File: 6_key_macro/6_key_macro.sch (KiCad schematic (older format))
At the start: 37 parts, among them J1 SWD, P1 USB_C_Plug_USB2.0, Q1 DMG1012T, SW1 CherryMX_LED, SW2 CherryMX_LED, SW3 CherryMX_LED, SW4 CherryMX_LED, SW5 CherryMX_LED, SW6 CherryMX_LED, SW7 Boot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

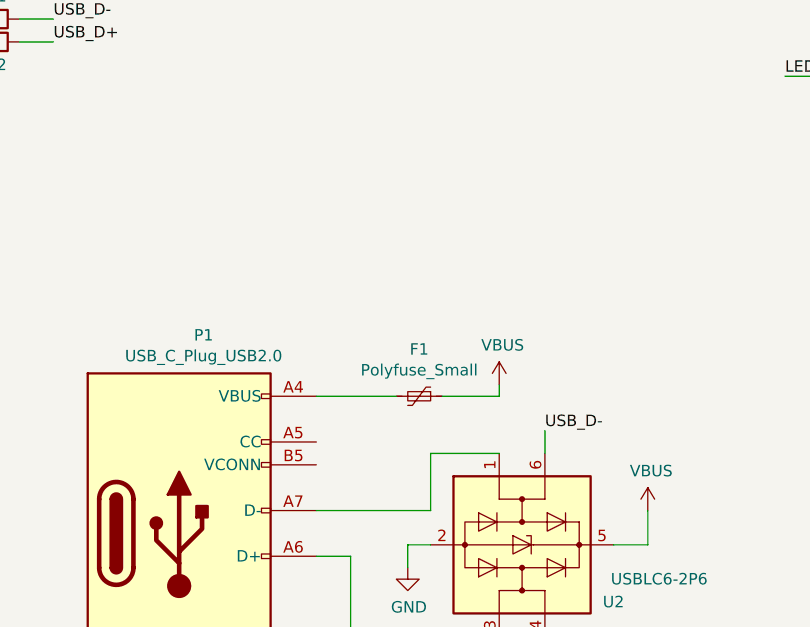
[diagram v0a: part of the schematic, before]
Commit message: added 5.1k resistors to cc1 and cc2 for usb-c to usb-c compatibility
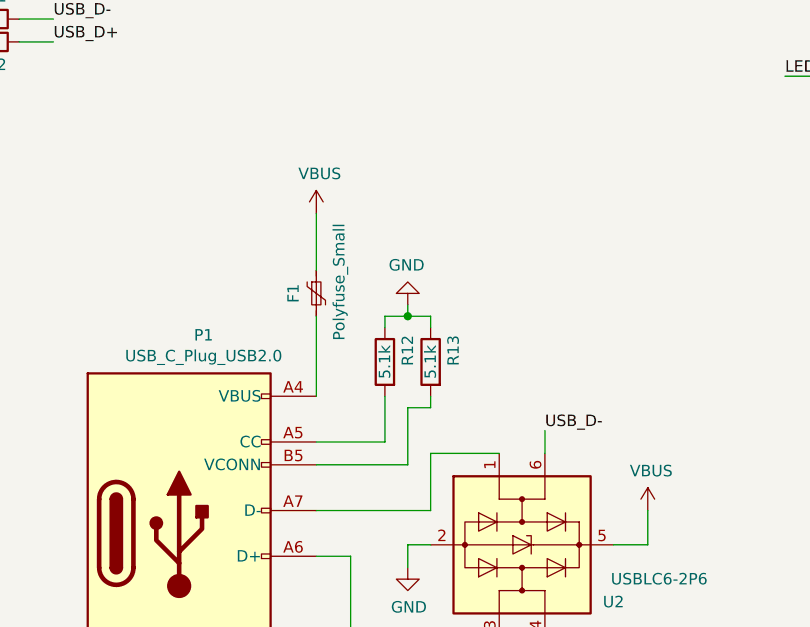
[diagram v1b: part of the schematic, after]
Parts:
- added R12, R13: 5.1k, Resistor_SMD:R_0805_2012Metric_Pad1.20x1.40mm_HandSolder, symbol Device:R
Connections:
- net GND: now also R12.1, R13.1
- net at P1.A5 (CC): now also R12.2
- net at P1.B5 (VCONN): now also R13.2
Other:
- moved on the sheet: F1
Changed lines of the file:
@@
 USB_D+
 Wire Wire Line
-	4400 5700 4750 5700
+	4400 5700 4400 5350
 $Comp
 L power:VBUS #PWR0109
 U 1 1 614AC2B7
-P 5200 5650
-F 0 "#PWR0109" H 5200 5500 50  0001 C CNN
-F 1 "VBUS" H 5215 5823 50  0000 C CNN
-F 2 "" H 5200 5650 50  0001 C CNN
-F 3 "" H 5200 5650 50  0001 C CNN
-	1    5200 5650
+P 4400 4900
+F 0 "#PWR0109" H 4400 4750 50  0001 C CNN
+F 1 "VBUS" H 4415 5073 50  0000 C CNN
+F 2 "" H 4400 4900 50  0001 C CNN
+F 3 "" H 4400 4900 50  0001 C CNN
+	1    4400 4900
 	1    0    0    -1
 $EndComp
@@
 L Device:Polyfuse_Small F1
 U 1 1 614F2940
-P 4850 5700
-F 0 "F1" V 4645 5700 50  0000 C CNN
-F 1 "Polyfuse_Small" V 4736 5700 50  0000 C CNN
-F 2 "Fuse:Fuse_0805_2012Metric_Pad1.15x1.40mm_HandSolder" H 4900 5500 50  0001 L CNN
-F 3 "~" H 4850 5700 50  0001 C CNN
-	1    4850 5700
-	0    1    1    0
-$EndComp
-Wire Wire Line
-	5200 5650 5200 5700
-Wire Wire Line
-	5200 5700 4950 5700
+P 4400 5250
+F 0 "F1" V 4300 5250 50  0000 C CNN
+F 1 "Polyfuse_Small" V 4500 5300 50  0000 C CNN
+F 2 "Fuse:Fuse_0805_2012Metric_Pad1.15x1.40mm_HandSolder" H 4450 5050 50  0001 L CNN
+F 3 "~" H 4400 5250 50  0001 C CNN
+	1    4400 5250
+	1    0    0    -1
+$EndComp
+Wire Wire Line
+	4400 4900 4400 5150
 $Comp
 L Device:Ferrite_Bead_Small FB1
@@
 Wire Wire Line
 	1000 5950 1650 5950
+$Comp
+L Device:R R12
+U 1 1 617771B9
+P 4700 5550
+F 0 "R12" V 4600 5600 50  0000 C CNN
+F 1 "5.1k" V 4700 5550 50  0000 C CNN
+F 2 "Resistor_SMD:R_0805_2012Metric_Pad1.20x1.40mm_HandSolder" V 4630 5550 50  0001 C CNN
+F 3 "~" H 4700 5550 50  0001 C CNN
+	1    4700 5550
+	-1   0    0    -1
+$EndComp
+$Comp
+L Device:R R13
+U 1 1 61783DEF
+P 4900 5550
+F 0 "R13" V 4800 5600 50  0000 C CNN
+F 1 "5.1k" V 4900 5550 50  0000 C CNN
+F 2 "Resistor_SMD:R_0805_2012Metric_Pad1.20x1.40mm_HandSolder" V 4830 5550 50  0001 C CNN
+F 3 "~" H 4900 5550 50  0001 C CNN
+	1    4900 5550
+	-1   0    0    -1
+$EndComp
+Wire Wire Line
+	4700 5900 4700 5700
+Wire Wire Line
+	4400 5900 4700 5900
+Wire Wire Line
+	4800 6000 4800 5750
+Wire Wire Line
+	4800 5750 4900 5750
+Wire Wire Line
+	4900 5750 4900 5700
+Wire Wire Line
+	4400 6000 4800 6000
+Wire Wire Line
+	4700 5400 4700 5350
+Wire Wire Line
+	4700 5350 4800 5350
+Wire Wire Line
+	4900 5350 4900 5400
+Wire Wire Line
+	4800 5350 4800 5300
+Connection ~ 4800 5350
+Wire Wire Line
+	4800 5350 4900 5350
+$Comp
+L power:GND #PWR0131
+U 1 1 617ACA32
+P 4800 5300
+F 0 "#PWR0131" H 4800 5050 50  0001 C CNN
+F 1 "GND" H 4805 5127 50  0000 C CNN
+F 2 "" H 4800 5300 50  0001 C CNN
+F 3 "" H 4800 5300 50  0001 C CNN
+	1    4800 5300
+	-1   0    0    1
+$EndComp
 $EndSCHEMATC

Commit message: swapped tvs diodes
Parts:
- removed U2: USBLC6-2P6, Package_TO_SOT_SMD:SOT-666, symbol Power_Protection:USBLC6-2P6
- added U2: USBLC6-2SC6, Package_TO_SOT_SMD:SOT-23-6, symbol Power_Protection:USBLC6-2SC6
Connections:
- net GND: now also U2.2 (GND)
- net USB_D+: now also U2.4 (I/O2)
- net USB_D-: now also U2.6 (I/O1)
- net VBUS: now also U2.5 (VBUS)
- net at P1.A6 (D+): now also U2.3 (I/O2)
- net at P1.A7 (D-): now also U2.1 (I/O1)
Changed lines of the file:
@@
 	1    0    0    -1
-$EndComp
-$Comp
-L Power_Protection:USBLC6-2P6 U2
-U 1 1 614DAD6B
-P 5300 6350
-F 0 "U2" V 5550 6750 50  0000 C CNN
-F 1 "USBLC6-2P6" V 5450 6950 50  0000 C CNN
-F 2 "Package_TO_SOT_SMD:SOT-666" H 5300 5850 50  0001 C CNN
-F 3 "https://www.st.com/resource/en/datasheet/usblc6-2.pdf" H 5500 6700 50  0001 C CNN
-	1    5300 6350
-	0    1    1    0
 $EndComp
 Wire Wire Line
@@
 	-1   0    0    1
 $EndComp
+$Comp
+L Power_Protection:USBLC6-2SC6 U2
+U 1 1 617CA8CA
+P 5300 6350
+F 0 "U2" V 5254 6794 50  0000 L CNN
+F 1 "USBLC6-2SC6" V 5345 6794 50  0000 L CNN
+F 2 "Package_TO_SOT_SMD:SOT-23-6" H 5300 5850 50  0001 C CNN
+F 3 "https://www.st.com/resource/en/datasheet/usblc6-2.pdf" H 5500 6700 50  0001 C CNN
+	1    5300 6350
+	0    1    1    0
+$EndComp
 $EndSCHEMATC
